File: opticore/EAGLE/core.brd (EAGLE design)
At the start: 90.1 x 77 mm, 67 parts, among them IC2 MC33269T-5.0, J1 POWER_JACKSLT, Q1 2N3904, Q2 2N3904, Q3 2N3904, Q4 2N3904, Q5 2N3904, Q6 2N3904, Q7 2N3904, X1 FFKV8

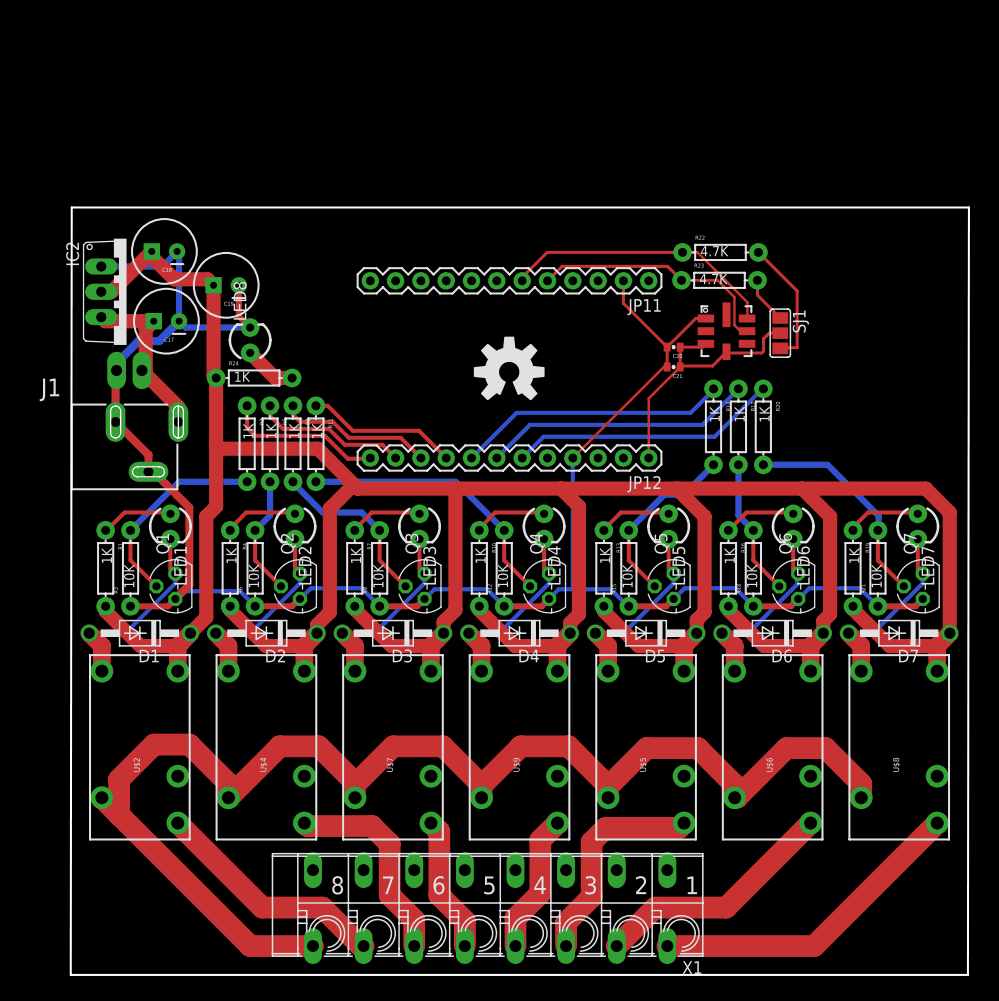
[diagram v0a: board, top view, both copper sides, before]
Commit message: Rewiring some things
Still haven't implemented 24V power supply.
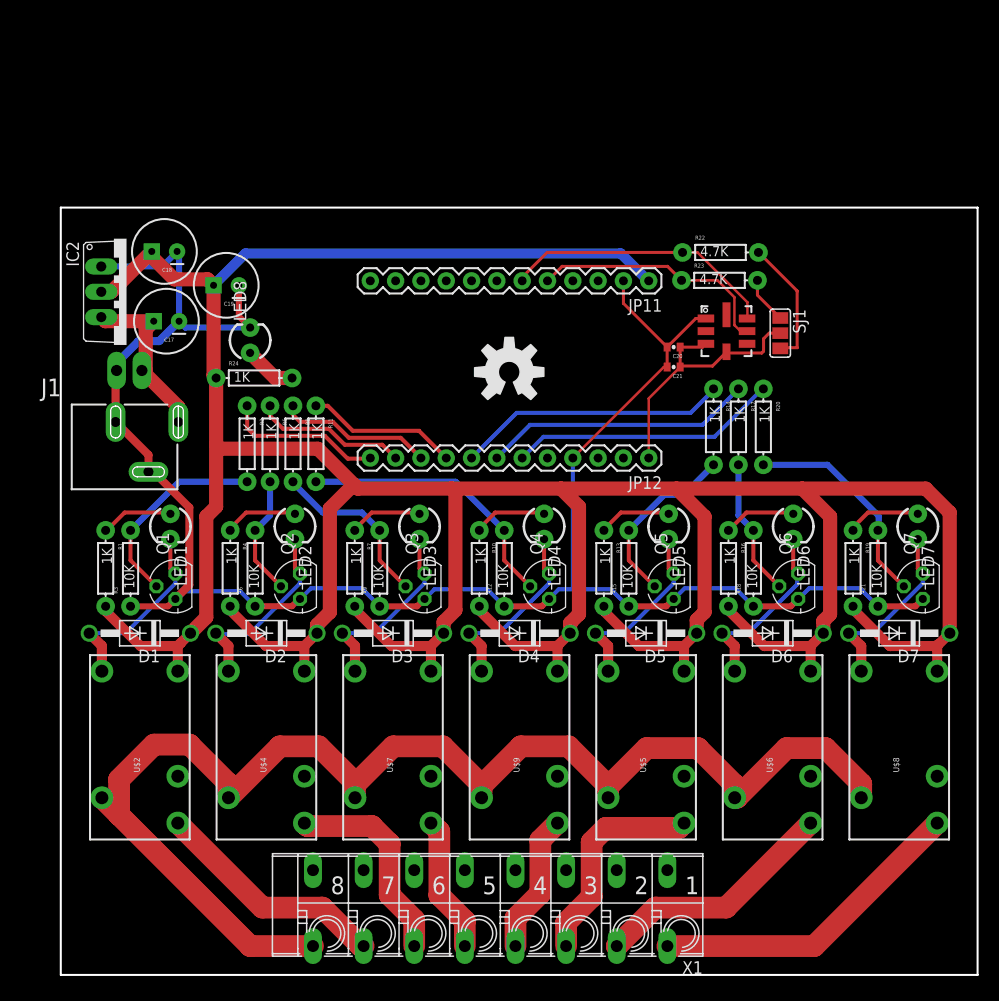
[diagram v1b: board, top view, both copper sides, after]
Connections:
- removed net RAW: JP11.1
- net 5V: now also JP11.1
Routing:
- net 5V: track 319.3 -> 365.4 mm
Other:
- board size 90.1 x 77 mm -> 92 x 77 mm

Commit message: Redoing power supply section
This isn't done yet. I still have to connect the 24VAC to the solenoids.
All GND pins on solenoids are tied together then to COMMON.
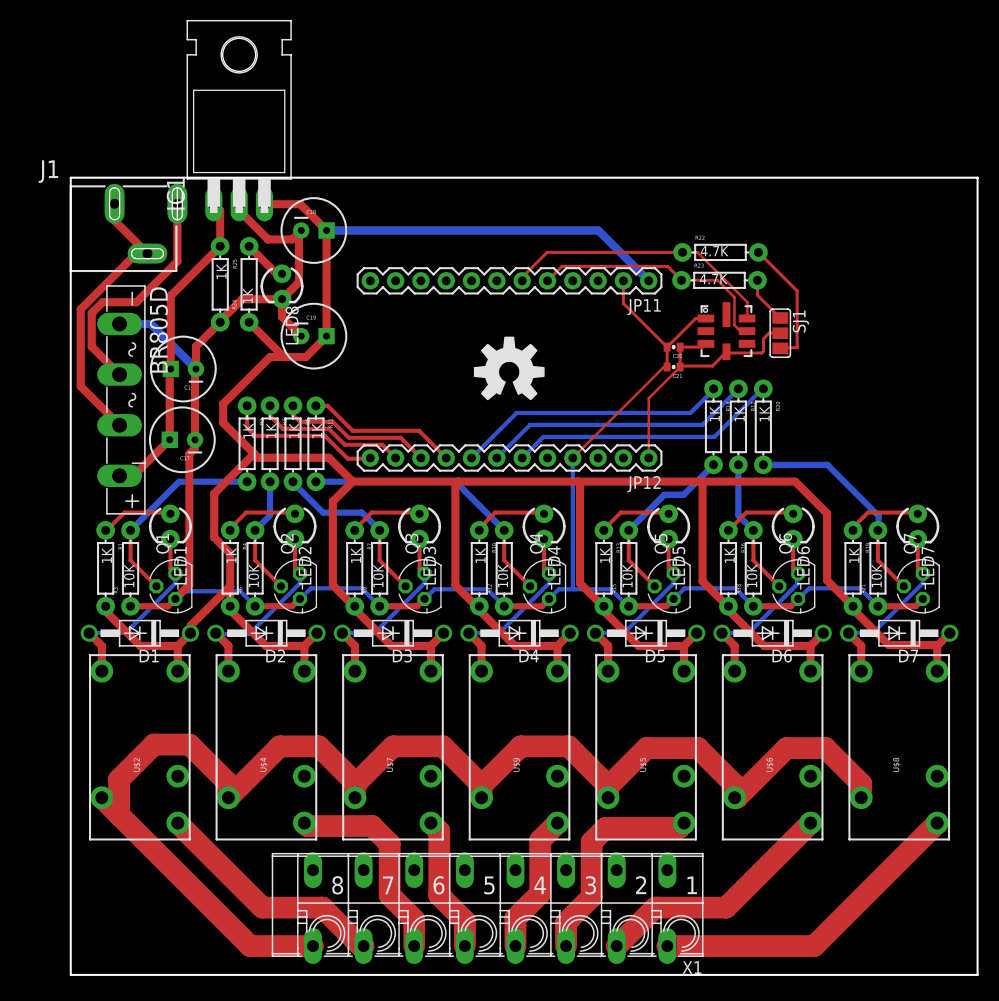
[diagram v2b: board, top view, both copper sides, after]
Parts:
- removed IC2: MC33269T-5.0, linear:TO220V
- removed JP10: M02PTH3, SparkFun-Connectors:1X02_LONGPADS
- added BR805D: (no value), rectifier:GBU4S
- added C1: 470uF, SparkFun-Passives:CPOL-RADIAL-100UF-25V
- added IC1: 7805T, adafruit:TO220H
- added R25: 1K, SparkFun-Resistors:AXIAL-0.3
- moved J1 21.9 mm to (-3.10, 80.0)
- moved C18 15.1 mm to (24.4, 74.7), turned to 0 degrees
- moved C17 12.0 mm to (11.2, 53.7)
- moved C19 10.2 mm to (24.4, 64.1), turned to 0 degrees
- moved R24 9.41 mm to (17.9, 69.3), turned to 90 degrees
- moved LED8 6.28 mm to (21.2, 69.1), turned to 270 degrees
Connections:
- removed net N$37: C17.1, IC2.3, J1.PWR, JP10.2
- new net 24VAC+: BR805D.AC1, J1.GND@1, J1.GND@2
- new net 24VAC-: BR805D.AC2, J1.PWR
- new net N$13: BR805D.+, C1.1, C17.1, IC1.1, R25.P$1
- net 5V: now also IC1.3; no longer IC2.2
- net GND: now also BR805D.-, C1.2, IC1.2, R25.P$2; no longer IC2.1, J1.GND@1, J1.GND@2, JP10.1
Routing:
- net 5V: track 365.4 -> 325.2 mm
- net N$13: track 0.00 -> 32.5 mm
- net 24VAC+: track 0.00 -> 28.6 mm
- net 24VAC-: track 0.00 -> 23.9 mm
- net N$37: track 17.8 -> 0.00 mm
- net GND: track 193.6 -> 197.6 mm
- net N$39: track 5.25 -> 4.44 mm
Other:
- board size 92 x 77 mm -> 91 x 80 mm

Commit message: Not sure
I haven't worked on this for a while. I assume it is trying to fix the
power problem. Still need to figure that out.
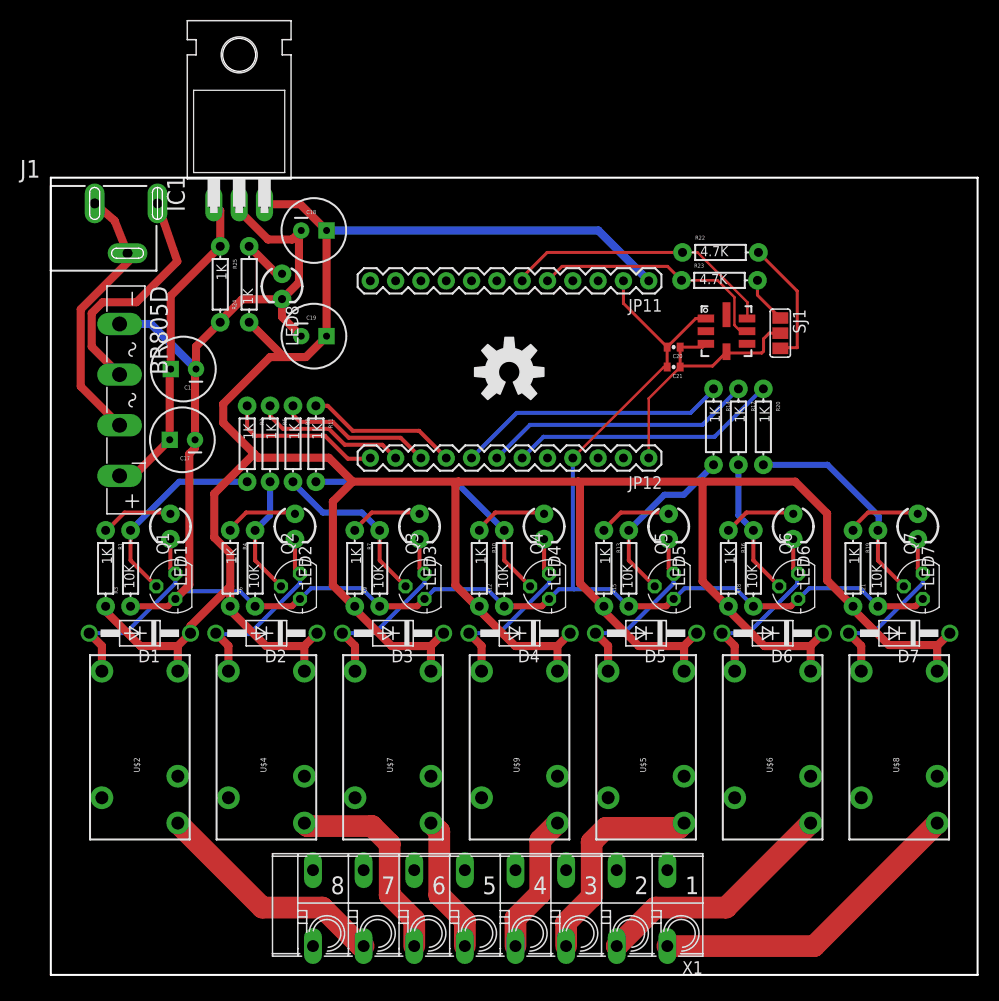
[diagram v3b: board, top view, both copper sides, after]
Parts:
- moved J1 2.00 mm to (-5.10, 80.0)
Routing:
- net MAIN: track 133.2 -> 0.00 mm
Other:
- board size 91 x 80 mm -> 93 x 80 mm
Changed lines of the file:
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@@
 <plain>
 <wire x1="91" y1="0" x2="91" y2="80" width="0.2032" layer="20"/>
-<wire x1="91" y1="80" x2="0" y2="80" width="0.2032" layer="20"/>
-<wire x1="91" y1="0" x2="0" y2="0" width="0.2032" layer="20"/>
-<wire x1="0" y1="0" x2="0" y2="80" width="0.2032" layer="20"/>
+<wire x1="91" y1="80" x2="-2" y2="80" width="0.2032" layer="20"/>
+<wire x1="91" y1="0" x2="-2" y2="0" width="0.2032" layer="20"/>
+<wire x1="-2" y1="0" x2="-2" y2="80" width="0.2032" layer="20"/>
 </plain>
 <attributes>
@@
 <element name="D4" library="diode" package="DO41-10" value="1N4004" x="45.0342" y="34.29" rot="R180"/>
 <element name="Q4" library="transistor-npn" package="TO92" value="2N3904" x="48" y="39" rot="R90"/>
-<element name="J1" library="SparkFun-Connectors" package="POWER_JACK_SLOT" value="POWER_JACKSLT" x="-3.1" y="79.9644" rot="R270"/>
+<element name="J1" library="SparkFun-Connectors" package="POWER_JACK_SLOT" value="POWER_JACKSLT" x="-5.1" y="80" rot="R270"/>
 <element name="C17" library="SparkFun-Passives" package="CPOL-RADIAL-100UF-25V" value="100uF" x="11.2" y="53.7" rot="R180"/>
 <element name="C18" library="SparkFun-Passives" package="CPOL-RADIAL-100UF-25V" value="100uF" x="24.4" y="74.7"/>
@@
 <contactref element="U$9" pad="4"/>
 <contactref element="X1" pad="8A"/>
-<wire x1="24.3078" y1="2.8956" x2="18.0086" y2="2.8956" width="2.1844" layer="1"/>
-<wire x1="18.0086" y1="2.8956" x2="4.8514" y2="16.0528" width="2.1844" layer="1"/>
-<wire x1="4.8514" y1="16.0528" x2="3.1242" y2="17.78" width="2.1844" layer="1"/>
-<wire x1="79.3242" y1="17.78" x2="79.3242" y2="19.177" width="2.1844" layer="1"/>
-<wire x1="79.3242" y1="19.177" x2="75.7428" y2="22.7584" width="2.1844" layer="1"/>
-<wire x1="66.6242" y1="17.78" x2="66.8528" y2="17.78" width="2.1844" layer="1"/>
-<wire x1="66.8528" y1="17.78" x2="71.8312" y2="22.7584" width="2.1844" layer="1"/>
-<wire x1="71.8312" y1="22.7584" x2="75.7428" y2="22.7584" width="2.1844" layer="1"/>
-<wire x1="66.6242" y1="17.78" x2="66.6242" y2="19.0754" width="2.1844" layer="1"/>
-<wire x1="66.6242" y1="19.0754" x2="62.9412" y2="22.7584" width="2.1844" layer="1"/>
-<wire x1="53.9242" y1="17.78" x2="53.9242" y2="18.9738" width="2.1844" layer="1"/>
-<wire x1="53.9242" y1="18.9738" x2="49.9618" y2="22.9362" width="2.1844" layer="1"/>
-<wire x1="41.2242" y1="17.78" x2="41.2242" y2="19.05" width="2.1844" layer="1"/>
-<wire x1="41.2242" y1="19.05" x2="37.338" y2="22.9362" width="2.1844" layer="1"/>
-<wire x1="28.5242" y1="17.78" x2="28.5242" y2="19.304" width="2.1844" layer="1"/>
-<wire x1="28.5242" y1="19.304" x2="24.892" y2="22.9362" width="2.1844" layer="1"/>
-<wire x1="20.9804" y1="22.9362" x2="24.892" y2="22.9362" width="2.1844" layer="1"/>
-<wire x1="28.5242" y1="19.304" x2="28.7274" y2="19.304" width="2.1844" layer="1"/>
-<wire x1="28.7274" y1="19.304" x2="32.3596" y2="22.9362" width="2.1844" layer="1"/>
-<wire x1="32.3596" y1="22.9362" x2="37.338" y2="22.9362" width="2.1844" layer="1"/>
-<wire x1="41.2242" y1="19.05" x2="41.275" y2="19.05" width="2.1844" layer="1"/>
-<wire x1="41.275" y1="19.05" x2="45.1612" y2="22.9362" width="2.1844" layer="1"/>
-<wire x1="45.1612" y1="22.9362" x2="49.9618" y2="22.9362" width="2.1844" layer="1"/>
-<wire x1="53.9242" y1="18.9738" x2="54.0004" y2="18.9738" width="2.1844" layer="1"/>
-<wire x1="54.0004" y1="18.9738" x2="57.785" y2="22.7584" width="2.1844" layer="1"/>
-<wire x1="57.785" y1="22.7584" x2="62.9412" y2="22.7584" width="2.1844" layer="1"/>
-<wire x1="15.8242" y1="17.78" x2="15.8242" y2="19.2024" width="2.1844" layer="1"/>
-<wire x1="15.8242" y1="19.2024" x2="11.9126" y2="23.114" width="2.1844" layer="1"/>
-<wire x1="4.8514" y1="16.0528" x2="4.8514" y2="19.6088" width="2.1844" layer="1"/>
-<wire x1="4.8514" y1="19.6088" x2="8.3566" y2="23.114" width="2.1844" layer="1"/>
-<wire x1="8.3566" y1="23.114" x2="11.9126" y2="23.114" width="2.1844" layer="1"/>
-<wire x1="15.8242" y1="17.78" x2="20.9804" y2="22.9362" width="2.1844" layer="1"/>
+<wire x1="66.6242" y1="17.78" x2="79.3242" y2="17.78" width="0" layer="19" extent="1-1"/>
+<wire x1="53.9242" y1="17.78" x2="66.6242" y2="17.78" width="0" layer="19" extent="1-1"/>
+<wire x1="41.2242" y1="17.78" x2="53.9242" y2="17.78" width="0" layer="19" extent="1-1"/>
+<wire x1="28.5242" y1="17.78" x2="41.2242" y2="17.78" width="0" layer="19" extent="1-1"/>
+<wire x1="15.8242" y1="17.78" x2="28.5242" y2="17.78" width="0" layer="19" extent="1-1"/>
+<wire x1="3.1242" y1="17.78" x2="15.8242" y2="17.78" width="0" layer="19" extent="1-1"/>
+<wire x1="24.3078" y1="2.8956" x2="28.5242" y2="17.78" width="0" layer="19" extent="1-1"/>
 </signal>
 <signal name="NO1">
@@
 <contactref element="J1" pad="GND@2"/>
 <contactref element="BR805D" pad="AC1"/>
-<wire x1="4.4" y1="77.3844" x2="4.4" y2="75.6844" width="0.8128" layer="1"/>
-<wire x1="4.4" y1="75.6844" x2="7.7" y2="72.3844" width="0.8128" layer="1"/>
-<wire x1="7.7" y1="72.3844" x2="6.5844" y2="72.3844" width="0.8128" layer="1"/>
+<wire x1="2.4" y1="77.42" x2="4.4" y2="75.6844" width="0.8128" layer="1"/>
+<wire x1="4.4" y1="75.6844" x2="5.7" y2="72.42" width="0.8128" layer="1"/>
+<wire x1="5.7" y1="72.42" x2="6.5844" y2="72.3844" width="0.8128" layer="1"/>
 <wire x1="6.5844" y1="72.3844" x2="1" y2="66.8" width="0.8128" layer="1"/>
 <wire x1="1" y1="66.8" x2="1" y2="59.06" width="0.8128" layer="1"/>
@@
 <contactref element="BR805D" pad="AC2"/>
 <contactref element="J1" pad="PWR"/>
-<wire x1="10.7" y1="77.3844" x2="10.7" y2="71.6" width="0.8128" layer="1"/>
+<wire x1="8.7" y1="77.42" x2="10.7" y2="71.6" width="0.8128" layer="1"/>
 <wire x1="10.7" y1="71.6" x2="6.6" y2="67.5" width="0.8128" layer="1"/>
 <wire x1="6.6" y1="67.5" x2="3.2" y2="67.5" width="0.8128" layer="1"/>
